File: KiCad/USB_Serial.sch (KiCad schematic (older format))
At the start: 34 parts, among them J15 USB_B_Mini, J16 USB_B_Micro, J17 AVR-ISP-6, J18 Conn_02x02_Odd_Even, U6 ATmega16U2-MU, Y2 16MHz

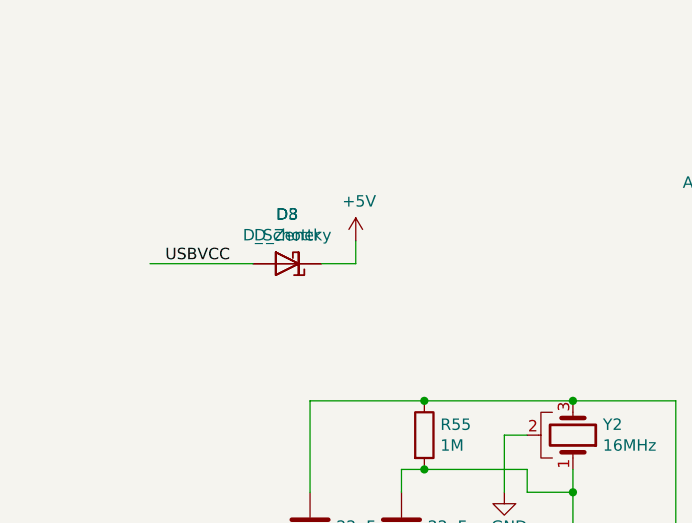
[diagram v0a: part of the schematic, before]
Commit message: removed D1 and D3, left Schottky diodes alone
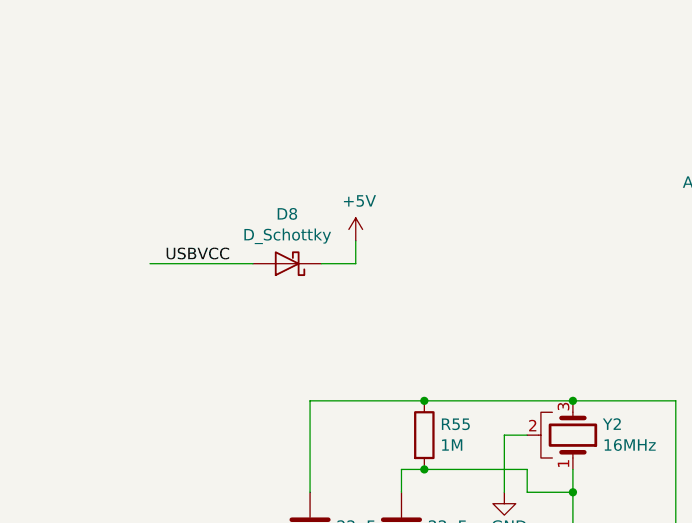
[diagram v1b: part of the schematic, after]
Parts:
- removed D3: D_Zener, Diode_SMD:D_SMB_Handsoldering, symbol Device:D_Zener
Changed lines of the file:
@@
 	2450 1700 2000 1700
-$Comp
-L Device:D_Zener D3
-U 1 1 5C49C1BC
-P 2600 1700
-F 0 "D3" H 2600 1484 50  0000 C CNN
-F 1 "D_Zener" H 2600 1575 50  0000 C CNN
-F 2 "Diode_SMD:D_SMB_Handsoldering" H 2600 1700 50  0001 C CNN
-F 3 "~" H 2600 1700 50  0001 C CNN
-F 4 "Micro Commercial" H 2600 1700 50  0001 C CNN "Manufacturer"
-F 5 "3SMBJ5925B-TP" H 2600 1700 50  0001 C CNN "Part Number"
-	1    2600 1700
-	-1   0    0    1
-$EndComp
 $Comp
 L power:+5V #PWR093

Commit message: tweaked ethernet
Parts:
- D8: footprint Diodes_SMD:D_SOD-323 -> Diode_SMD:D_SOD-323
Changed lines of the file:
@@
 F 0 "D8" H 2600 1484 50  0000 C CNN
 F 1 "D_Schottky" H 2600 1575 50  0000 C CNN
-F 2 "Diodes_SMD:D_SOD-323" H 2600 1700 50  0001 C CNN
+F 2 "Diode_SMD:D_SOD-323" H 2600 1700 50  0001 C CNN
 F 3 "~" H 2600 1700 50  0001 C CNN
 F 4 "Toshiba Semiconductor and Storage" H 2600 1700 50  0001 C CNN "Manufacturer"

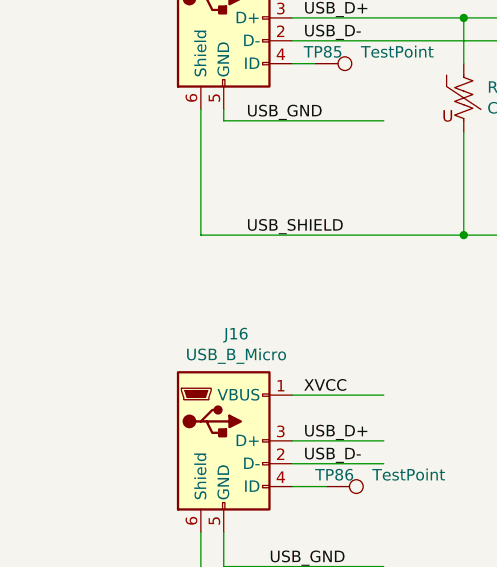
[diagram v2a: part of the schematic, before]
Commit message: added footprints for Y3 FB1 FB3 FB2 F1
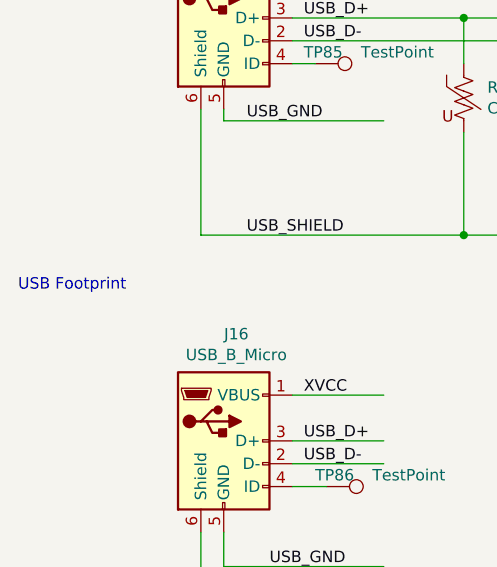
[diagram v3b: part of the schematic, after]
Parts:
- FB1: footprint Inductors_SMD:L_0603_HandSoldering -> Inductor_SMD:L_0603_1608Metric_Pad1.05x0.95mm_HandSolder
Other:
- note added: "USB Footprint"
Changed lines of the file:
@@
 F 0 "FB1" V 3600 5200 50  0000 C CNN
 F 1 "600R@100MHz" V 3600 5700 50  0000 C CNN
-F 2 "Inductors_SMD:L_0603_HandSoldering" V 3680 5300 50  0001 C CNN
+F 2 "Inductor_SMD:L_0603_1608Metric_Pad1.05x0.95mm_HandSolder" V 3680 5300 50  0001 C CNN
 F 3 "~" H 3750 5300 50  0001 C CNN
 F 4 "TDK" H 3750 5300 50  0001 C CNN "Manufacturer"
@@
 Text Label 6200 4600 0    50   ~ 0
 MICRO_RX
+Text Notes 750  5550 0    50   ~ 0
+USB Footprint
 $EndSCHEMATC

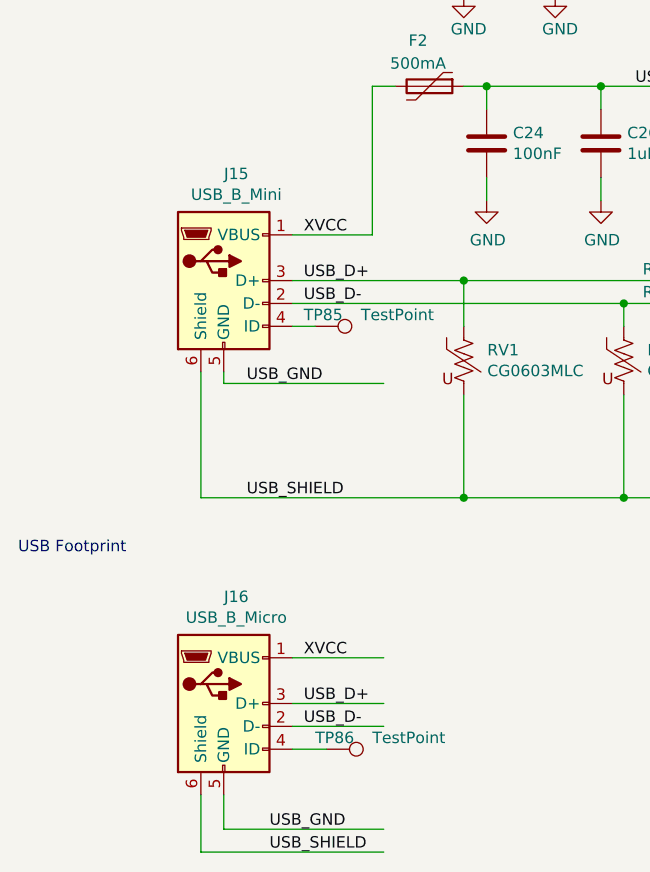
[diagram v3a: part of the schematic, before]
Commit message: created footprint for USB micro, linked to J16
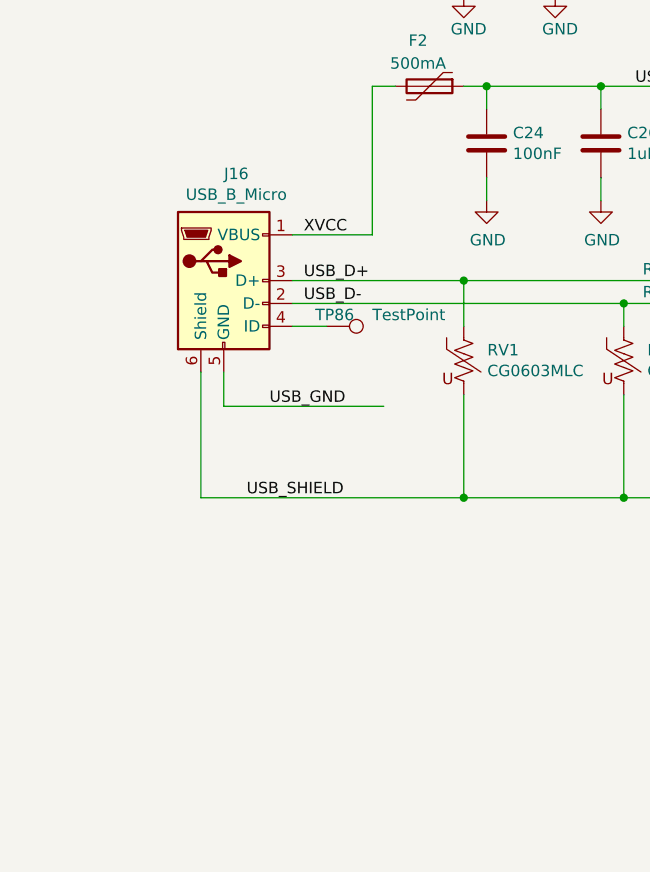
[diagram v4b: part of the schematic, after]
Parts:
- removed J15: USB_B_Mini, Connector_USB:USB_Mini-B_Lumberg_2486_01_Horizontal, symbol Connector:USB_B_Mini
- removed TP85: TestPoint, TestPoint:TestPoint_THTPad_D1.0mm_Drill0.5mm, symbol Connector:TestPoint
- J16: footprint (none) -> Snack Machine:Amphenol_10118193-0001LF; Manufacturer (none) -> Amphenol FCI; Part Number (none) -> 10118193-0001LF
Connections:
- wire segments 116 -> 108
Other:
- note removed: "USB Footprint"
- moved on the sheet: J16, TP86
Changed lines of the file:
@@
 	7400 5000 8000 5000
-$Comp
-L Connector:USB_B_Mini J15
-U 1 1 5BF070B3
-P 1650 4350
-F 0 "J15" H 1705 4817 50  0000 C CNN
-F 1 "USB_B_Mini" H 1705 4726 50  0000 C CNN
-F 2 "Connector_USB:USB_Mini-B_Lumberg_2486_01_Horizontal" H 1800 4300 50  0001 C CNN
-F 3 "~" H 1800 4300 50  0001 C CNN
-	1    1650 4350
-	1    0    0    -1
-$EndComp
 $Comp
 L Connector:USB_B_Micro J16
 U 1 1 5BF07281
-P 1650 6200
-F 0 "J16" H 1705 6667 50  0000 C CNN
-F 1 "USB_B_Micro" H 1705 6576 50  0000 C CNN
-F 2 "" H 1800 6150 50  0001 C CNN
-F 3 "~" H 1800 6150 50  0001 C CNN
-	1    1650 6200
+P 1650 4350
+F 0 "J16" H 1705 4817 50  0000 C CNN
+F 1 "USB_B_Micro" H 1705 4726 50  0000 C CNN
+F 2 "Snack Machine:Amphenol_10118193-0001LF" H 1800 4300 50  0001 C CNN
+F 3 "~" H 1800 4300 50  0001 C CNN
+F 4 "Amphenol FCI" H 1650 4350 50  0001 C CNN "Manufacturer"
+F 5 "10118193-0001LF" H 1650 4350 50  0001 C CNN "Part Number"
+	1    1650 4350
 	1    0    0    -1
 $EndComp
@@
 USB_D-
 Wire Wire Line
-	1950 6000 2350 6000
-Wire Wire Line
-	1950 6200 2350 6200
-Wire Wire Line
-	1950 6300 2350 6300
-Wire Wire Line
-	1950 6400 2100 6400
-Wire Wire Line
-	1950 4550 2050 4550
-Text Label 2000 6000 0    50   ~ 0
-XVCC
-Text Label 2000 6200 0    50   ~ 0
-USB_D+
-Text Label 2000 6300 0    50   ~ 0
-USB_D-
-Wire Wire Line
-	1650 4750 1650 4800
-Wire Wire Line
-	1650 4800 2350 4800
-Text Label 1750 4800 0    50   ~ 0
-USB_GND
-Wire Wire Line
-	1650 6600 1650 6750
-Wire Wire Line
-	1650 6750 2350 6750
-Text Label 1850 6750 0    50   ~ 0
+	1950 4550 2100 4550
+Wire Wire Line
+	1650 4750 1650 4900
+Wire Wire Line
+	1650 4900 2350 4900
+Text Label 1850 4900 0    50   ~ 0
 USB_GND
 $Comp
 L Connector:TestPoint TP86
 U 1 1 5BF1286E
-P 2100 6400
-F 0 "TP86" V 2050 6350 50  0000 L CNN
-F 1 "TestPoint" V 2050 6600 50  0000 L CNN
-F 2 "TestPoint:TestPoint_THTPad_D1.0mm_Drill0.5mm" H 2300 6400 50  0001 C CNN
-F 3 "~" H 2300 6400 50  0001 C CNN
-	1    2100 6400
+P 2100 4550
+F 0 "TP86" V 2050 4500 50  0000 L CNN
+F 1 "TestPoint" V 2050 4750 50  0000 L CNN
+F 2 "TestPoint:TestPoint_THTPad_D1.0mm_Drill0.5mm" H 2300 4550 50  0001 C CNN
+F 3 "~" H 2300 4550 50  0001 C CNN
+	1    2100 4550
 	0    1    1    0
 $EndComp
-$Comp
-L Connector:TestPoint TP85
-U 1 1 5BF144D7
-P 2050 4550
-F 0 "TP85" V 2000 4500 50  0000 L CNN
-F 1 "TestPoint" V 2000 4750 50  0000 L CNN
-F 2 "TestPoint:TestPoint_THTPad_D1.0mm_Drill0.5mm" H 2250 4550 50  0001 C CNN
-F 3 "~" H 2250 4550 50  0001 C CNN
-	1    2050 4550
-	0    1    1    0
-$EndComp
-Wire Wire Line
-	1550 6600 1550 6850
-Wire Wire Line
-	1550 6850 2350 6850
-Text Label 1850 6850 0    50   ~ 0
-USB_SHIELD
 Wire Wire Line
 	1550 4750 1550 5300
@@
 Text Label 6200 4600 0    50   ~ 0
 MICRO_RX
-Text Notes 750  5550 0    50   ~ 0
-USB Footprint
 $EndSCHEMATC

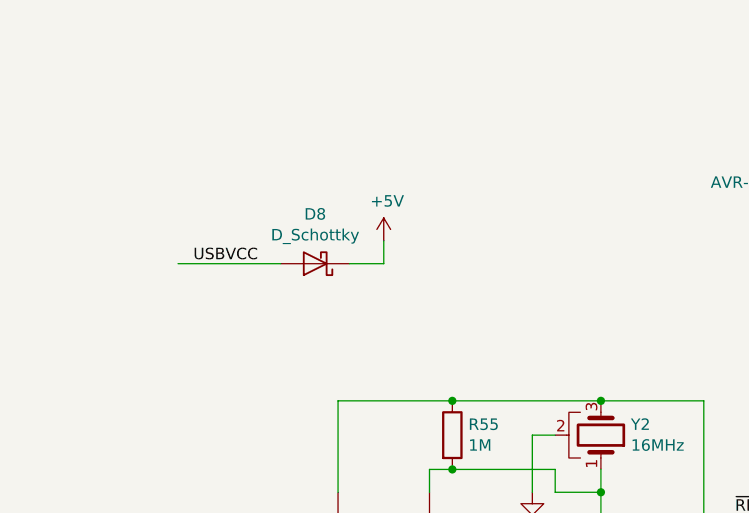
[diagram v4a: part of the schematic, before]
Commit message: updated motor drive circuitry, annotated
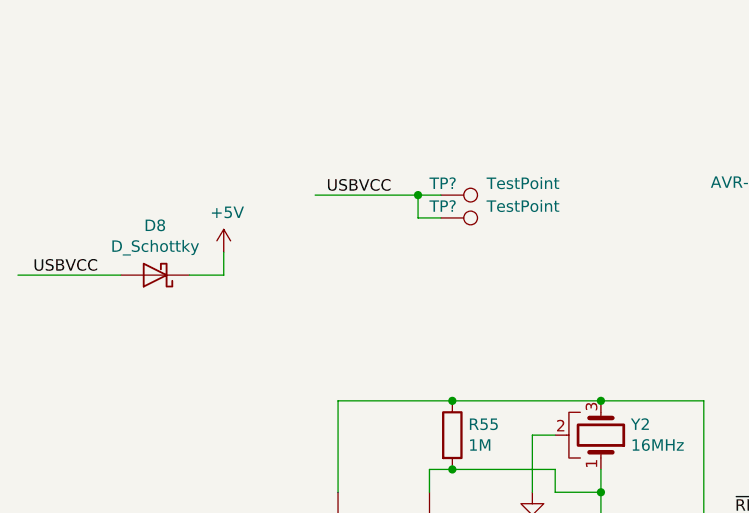
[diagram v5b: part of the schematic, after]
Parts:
- added TP? (x2): TestPoint, TestPoint:TestPoint_THTPad_D1.0mm_Drill0.5mm, symbol Connector:TestPoint
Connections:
- wire segments 108 -> 112
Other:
- moved on the sheet: D8
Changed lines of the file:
@@
 Text Label 6450 5000 0    50   ~ 0
 DTR
-Text Label 2350 1700 2    50   ~ 0
+Text Label 1650 1750 2    50   ~ 0
 USBVCC
 Wire Wire Line
-	2450 1700 2000 1700
+	1750 1750 1300 1750
 $Comp
 L power:+5V #PWR093
 U 1 1 5C4A9D62
-P 2900 1600
-F 0 "#PWR093" H 2900 1450 50  0001 C CNN
-F 1 "+5V" H 2915 1773 50  0000 C CNN
-F 2 "" H 2900 1600 50  0001 C CNN
-F 3 "" H 2900 1600 50  0001 C CNN
-	1    2900 1600
+P 2200 1650
+F 0 "#PWR093" H 2200 1500 50  0001 C CNN
+F 1 "+5V" H 2215 1823 50  0000 C CNN
+F 2 "" H 2200 1650 50  0001 C CNN
+F 3 "" H 2200 1650 50  0001 C CNN
+	1    2200 1650
 	1    0    0    -1
 $EndComp
 Wire Wire Line
-	2900 1700 2900 1600
+	2200 1750 2200 1650
 Wire Wire Line
 	5500 2350 5500 2400
@@
 	3200 2600 3650 2600
 Wire Wire Line
-	2750 1700 2900 1700
+	2050 1750 2200 1750
 $Comp
 L Device:D_Schottky D8
 U 1 1 5C21EC9A
-P 2600 1700
-F 0 "D8" H 2600 1484 50  0000 C CNN
-F 1 "D_Schottky" H 2600 1575 50  0000 C CNN
-F 2 "Diode_SMD:D_SOD-323" H 2600 1700 50  0001 C CNN
-F 3 "~" H 2600 1700 50  0001 C CNN
-F 4 "Toshiba Semiconductor and Storage" H 2600 1700 50  0001 C CNN "Manufacturer"
-F 5 "CUS08F30,H3F" H 2600 1700 50  0001 C CNN "Part Number"
-	1    2600 1700
+P 1900 1750
+F 0 "D8" H 1900 1534 50  0000 C CNN
+F 1 "D_Schottky" H 1900 1625 50  0000 C CNN
+F 2 "Diode_SMD:D_SOD-323" H 1900 1750 50  0001 C CNN
+F 3 "~" H 1900 1750 50  0001 C CNN
+F 4 "Toshiba Semiconductor and Storage" H 1900 1750 50  0001 C CNN "Manufacturer"
+F 5 "CUS08F30,H3F" H 1900 1750 50  0001 C CNN "Part Number"
+	1    1900 1750
 	-1   0    0    1
 $EndComp
@@
 Text Label 6200 4600 0    50   ~ 0
 MICRO_RX
+Text Label 2650 1400 0    50   ~ 0
+USBVCC
+Wire Wire Line
+	2600 1400 3050 1400
+$Comp
+L Connector:TestPoint TP?
+U 1 1 5C3B0CCE
+P 3150 1500
+AR Path="/5BCD883C/5C3B0CCE" Ref="TP?"  Part="1"
+AR Path="/5C3B0CCE" Ref="TP?"  Part="1"
+F 0 "TP?" V 3100 1450 50  0000 L CNN
+F 1 "TestPoint" V 3100 1700 50  0000 L CNN
+F 2 "TestPoint:TestPoint_THTPad_D1.0mm_Drill0.5mm" H 3350 1500 50  0001 C CNN
+F 3 "~" H 3350 1500 50  0001 C CNN
+	1    3150 1500
+	0    1    1    0
+$EndComp
+$Comp
+L Connector:TestPoint TP?
+U 1 1 5C3B7E84
+P 3150 1400
+AR Path="/5BCD883C/5C3B7E84" Ref="TP?"  Part="1"
+AR Path="/5C3B7E84" Ref="TP?"  Part="1"
+F 0 "TP?" V 3100 1350 50  0000 L CNN
+F 1 "TestPoint" V 3100 1600 50  0000 L CNN
+F 2 "TestPoint:TestPoint_THTPad_D1.0mm_Drill0.5mm" H 3350 1400 50  0001 C CNN
+F 3 "~" H 3350 1400 50  0001 C CNN
+	1    3150 1400
+	0    1    1    0
+$EndComp
+Wire Wire Line
+	3050 1400 3050 1500
+Wire Wire Line
+	3050 1500 3150 1500
+Connection ~ 3050 1400
+Wire Wire Line
+	3050 1400 3150 1400
 $EndSCHEMATC

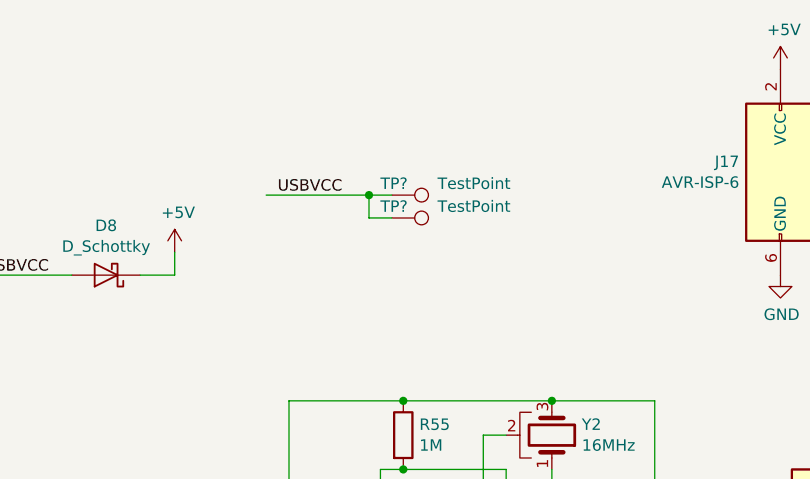
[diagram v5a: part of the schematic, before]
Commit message: fixed S2A and motor drive capacitor footprint links
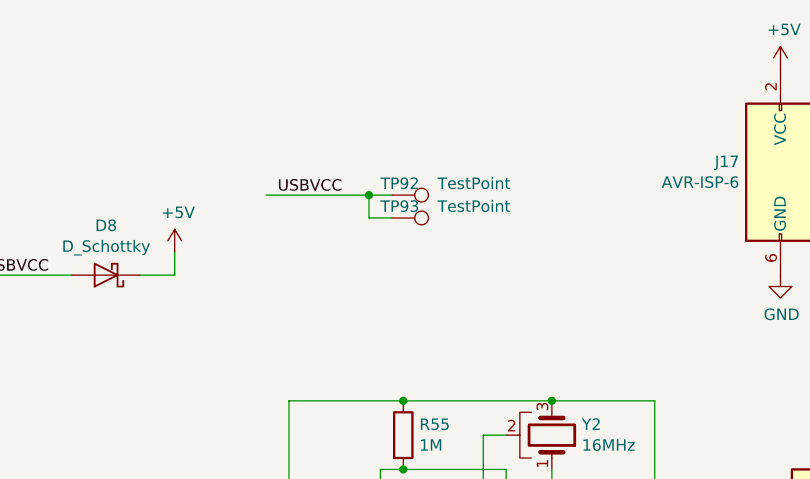
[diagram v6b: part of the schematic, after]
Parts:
- gave numbers to parts that had none: 2
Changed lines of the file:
@@
 	2600 1400 3050 1400
 $Comp
-L Connector:TestPoint TP?
+L Connector:TestPoint TP93
 U 1 1 5C3B0CCE
 P 3150 1500
-AR Path="/5BCD883C/5C3B0CCE" Ref="TP?"  Part="1"
+AR Path="/5BCD883C/5C3B0CCE" Ref="TP93"  Part="1"
 AR Path="/5C3B0CCE" Ref="TP?"  Part="1"
-F 0 "TP?" V 3100 1450 50  0000 L CNN
+F 0 "TP93" V 3100 1450 50  0000 L CNN
 F 1 "TestPoint" V 3100 1700 50  0000 L CNN
 F 2 "TestPoint:TestPoint_THTPad_D1.0mm_Drill0.5mm" H 3350 1500 50  0001 C CNN
@@
 $EndComp
 $Comp
-L Connector:TestPoint TP?
+L Connector:TestPoint TP92
 U 1 1 5C3B7E84
 P 3150 1400
-AR Path="/5BCD883C/5C3B7E84" Ref="TP?"  Part="1"
+AR Path="/5BCD883C/5C3B7E84" Ref="TP92"  Part="1"
 AR Path="/5C3B7E84" Ref="TP?"  Part="1"
-F 0 "TP?" V 3100 1350 50  0000 L CNN
+F 0 "TP92" V 3100 1350 50  0000 L CNN
 F 1 "TestPoint" V 3100 1600 50  0000 L CNN
 F 2 "TestPoint:TestPoint_THTPad_D1.0mm_Drill0.5mm" H 3350 1400 50  0001 C CNN

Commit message: rearranging footprints on layout
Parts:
- TP86, TP92, TP93: footprint TestPoint:TestPoint_THTPad_D1.0mm_Drill0.5mm -> Snack Machine:TestPoint_THTPad_D0.8mm_Drill0.4mm
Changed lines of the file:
@@
 F 0 "TP86" V 2050 4500 50  0000 L CNN
 F 1 "TestPoint" V 2050 4750 50  0000 L CNN
-F 2 "TestPoint:TestPoint_THTPad_D1.0mm_Drill0.5mm" H 2300 4550 50  0001 C CNN
+F 2 "Snack Machine:TestPoint_THTPad_D0.8mm_Drill0.4mm" H 2300 4550 50  0001 C CNN
 F 3 "~" H 2300 4550 50  0001 C CNN
 	1    2100 4550
@@
 F 0 "TP93" V 3100 1450 50  0000 L CNN
 F 1 "TestPoint" V 3100 1700 50  0000 L CNN
-F 2 "TestPoint:TestPoint_THTPad_D1.0mm_Drill0.5mm" H 3350 1500 50  0001 C CNN
+F 2 "Snack Machine:TestPoint_THTPad_D0.8mm_Drill0.4mm" H 3350 1500 50  0001 C CNN
 F 3 "~" H 3350 1500 50  0001 C CNN
 	1    3150 1500
@@
 F 0 "TP92" V 3100 1350 50  0000 L CNN
 F 1 "TestPoint" V 3100 1600 50  0000 L CNN
-F 2 "TestPoint:TestPoint_THTPad_D1.0mm_Drill0.5mm" H 3350 1400 50  0001 C CNN
+F 2 "Snack Machine:TestPoint_THTPad_D0.8mm_Drill0.4mm" H 3350 1400 50  0001 C CNN
 F 3 "~" H 3350 1400 50  0001 C CNN
 	1    3150 1400
